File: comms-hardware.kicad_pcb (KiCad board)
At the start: 4 copper layers, 92.5 x 92.5 mm, 314 parts, among them U1 TXCO_TG_5021CG, U10 CC1120, U12 ADT7420, U14 OPA320, U16 RF5110G, U18 FA_128_, U2 TPS79930, U3 FA_128_, U4 CC1120, U5 STM32F407VG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

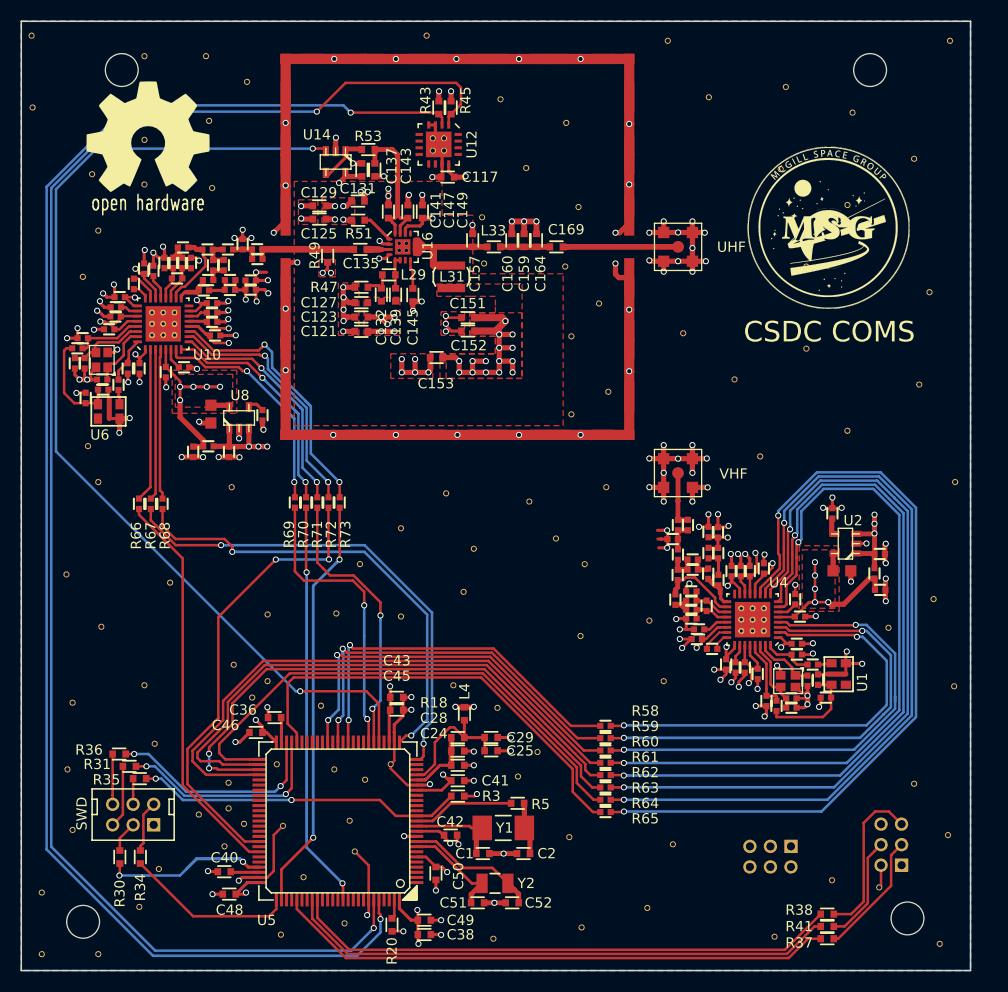
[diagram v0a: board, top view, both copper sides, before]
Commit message: Generated BOM, Fixed Mouting Holes dimensions and positions, Fixed 3D Libraries references
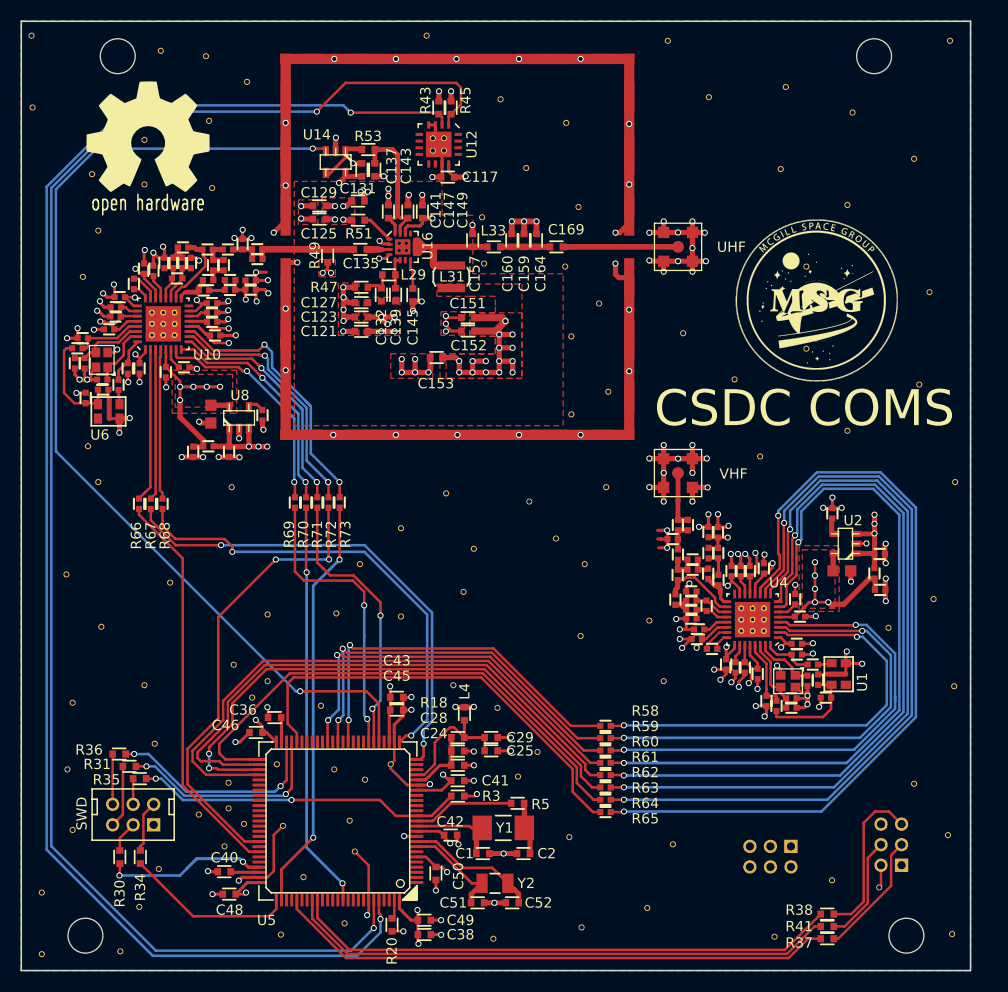
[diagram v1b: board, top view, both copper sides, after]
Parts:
- REF** (x4): value MountingHole_3mm -> MountingHole_3.4mm
- moved G*** 7.17 mm to (180.1, 81.8)
- moved REF** 6.66 mm to (185.4, 145.6)
